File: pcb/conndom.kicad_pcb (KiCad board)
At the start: 2 copper layers, 91 x 30 mm, 18 parts, among them J1 USB C PWR, J2 USB A WIFI

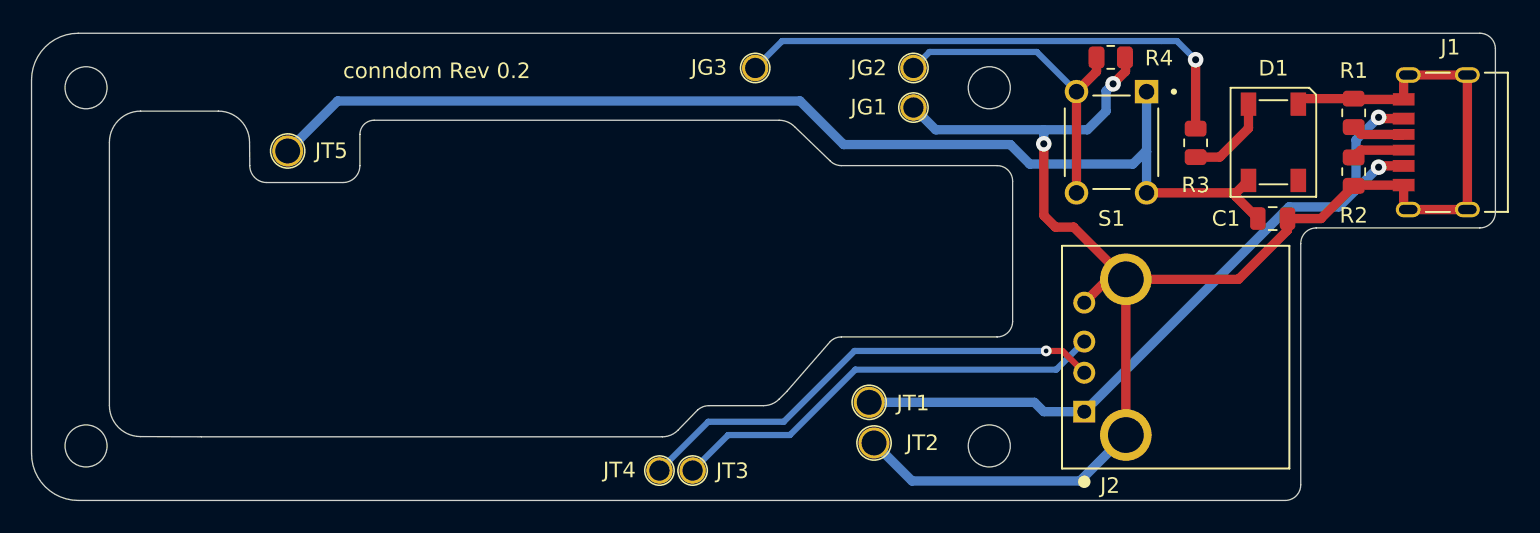
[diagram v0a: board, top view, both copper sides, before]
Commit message: new pcb layout with castellated holes
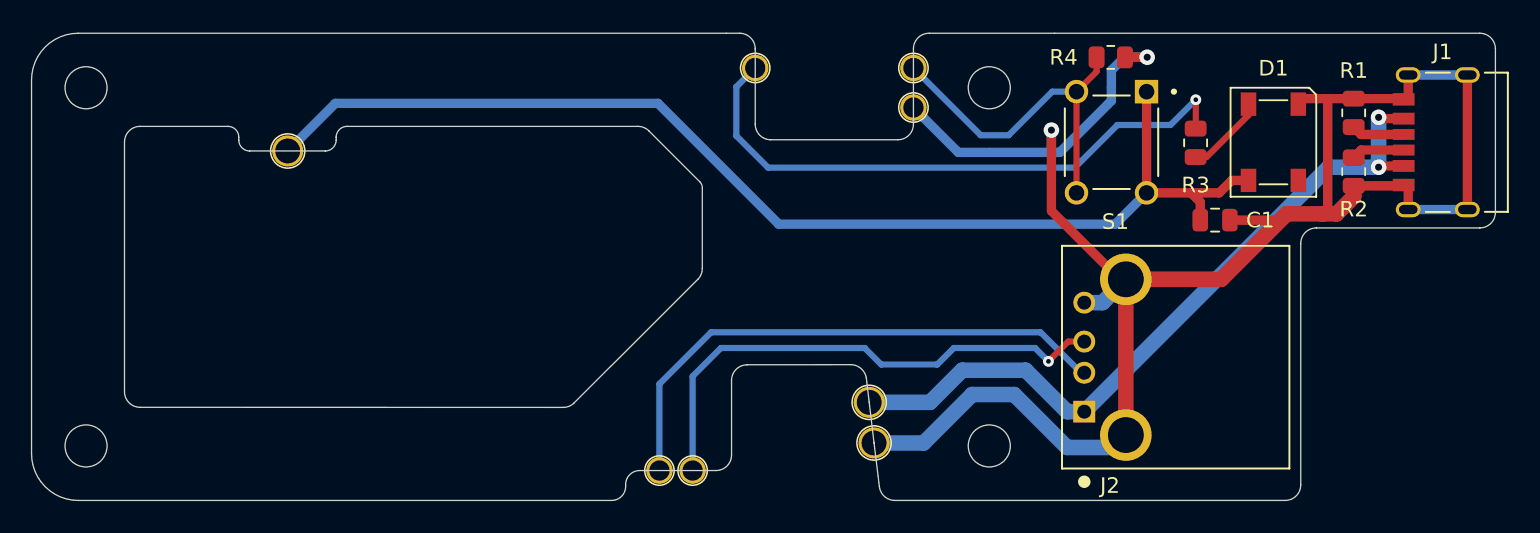
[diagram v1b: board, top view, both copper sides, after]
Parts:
- moved C1 3.70 mm to (168.0, 92.0)
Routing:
- net GND: track 108.9 -> 124.9 mm
- net Net-(JT3-Pin_1): track 28.6 -> 33.7 mm, vias 0 -> 1
- net Net-(JG3-Pin_1): track 34.0 -> 38.9 mm
- net Net-(JT4-Pin_1): track 31.0 -> 35.3 mm, vias 1 -> 0
- net Net-(D1-VDD): track 74.1 -> 75.8 mm
- net Net-(JG2-Pin_1): track 21.2 -> 22.7 mm
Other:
- outline, holes or cut-outs redrawn
- board text added: "conndom PCB 0.3"
- board text removed: "conndom Rev 0.2"
